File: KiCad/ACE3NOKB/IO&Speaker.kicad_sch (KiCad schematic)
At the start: 22 parts, among them Q3 BC183

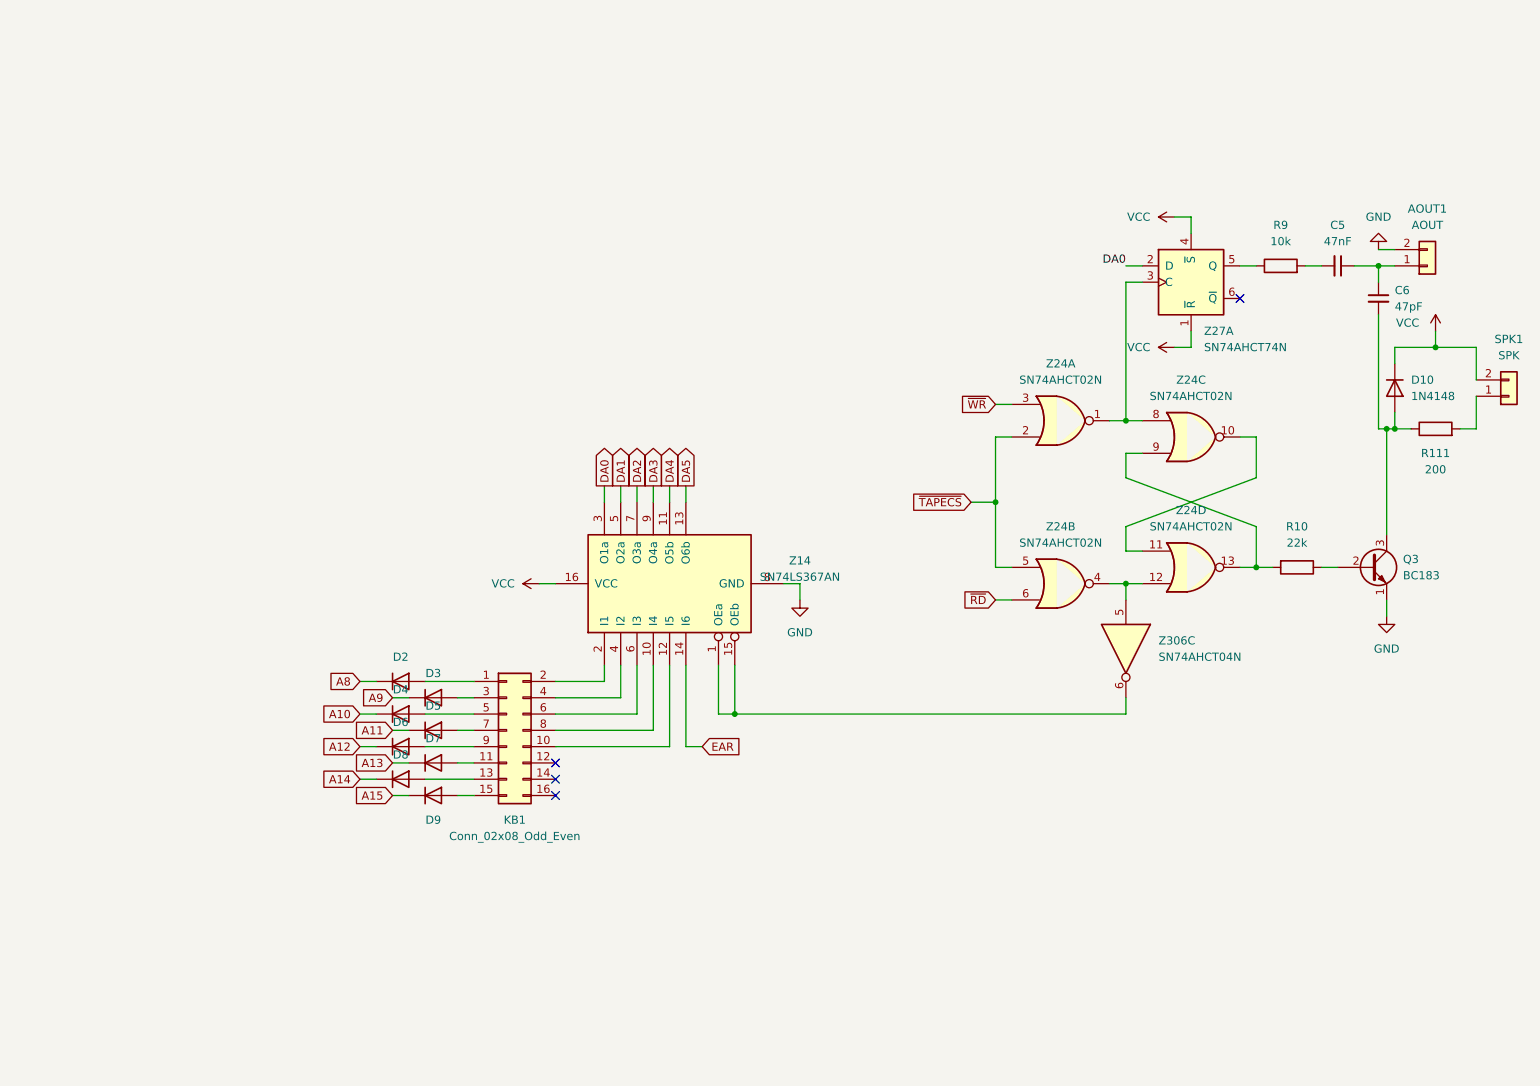
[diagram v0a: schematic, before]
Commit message: Update to latest symbols. Change name of Data Bus from DA to D.
Signed-off-by: John Bradley <flypie@rocketmail.com>
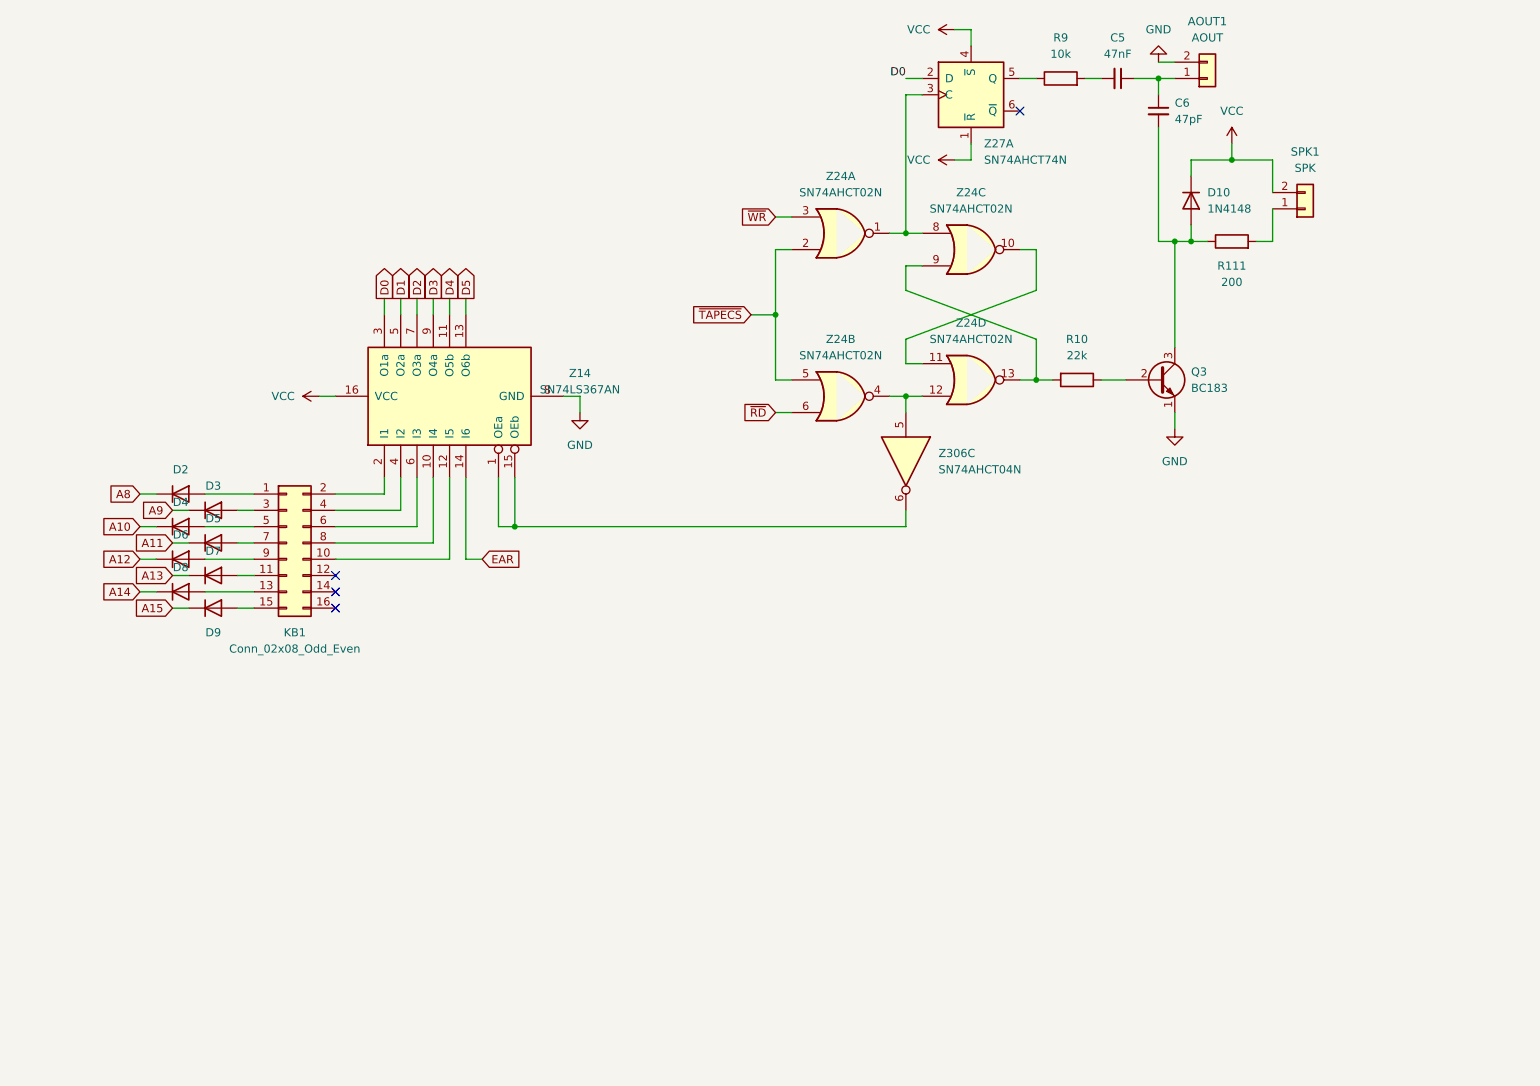
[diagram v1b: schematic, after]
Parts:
- D10: footprint Diode_THT:D_DO-35_SOD27_P2.54mm_Vertical_AnodeUp -> Diode_THT:D_DO-35_SOD27_P7.62mm_Horizontal
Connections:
- net DA0 renamed D0
- net DA1 renamed D1
- net DA2 renamed D2
- net DA3 renamed D3
- net DA4 renamed D4
- net DA5 renamed D5
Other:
- moved on the sheet: AOUT1, C5, C6, D10, D2, D3, D4, D5, D6, D7, D8, D9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

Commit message: Consolidation with increased configuration of speed and Int Routing to allow Orginal ACE ROM.
Signed-off-by: John Bradley <flypie@rocketmail.com>
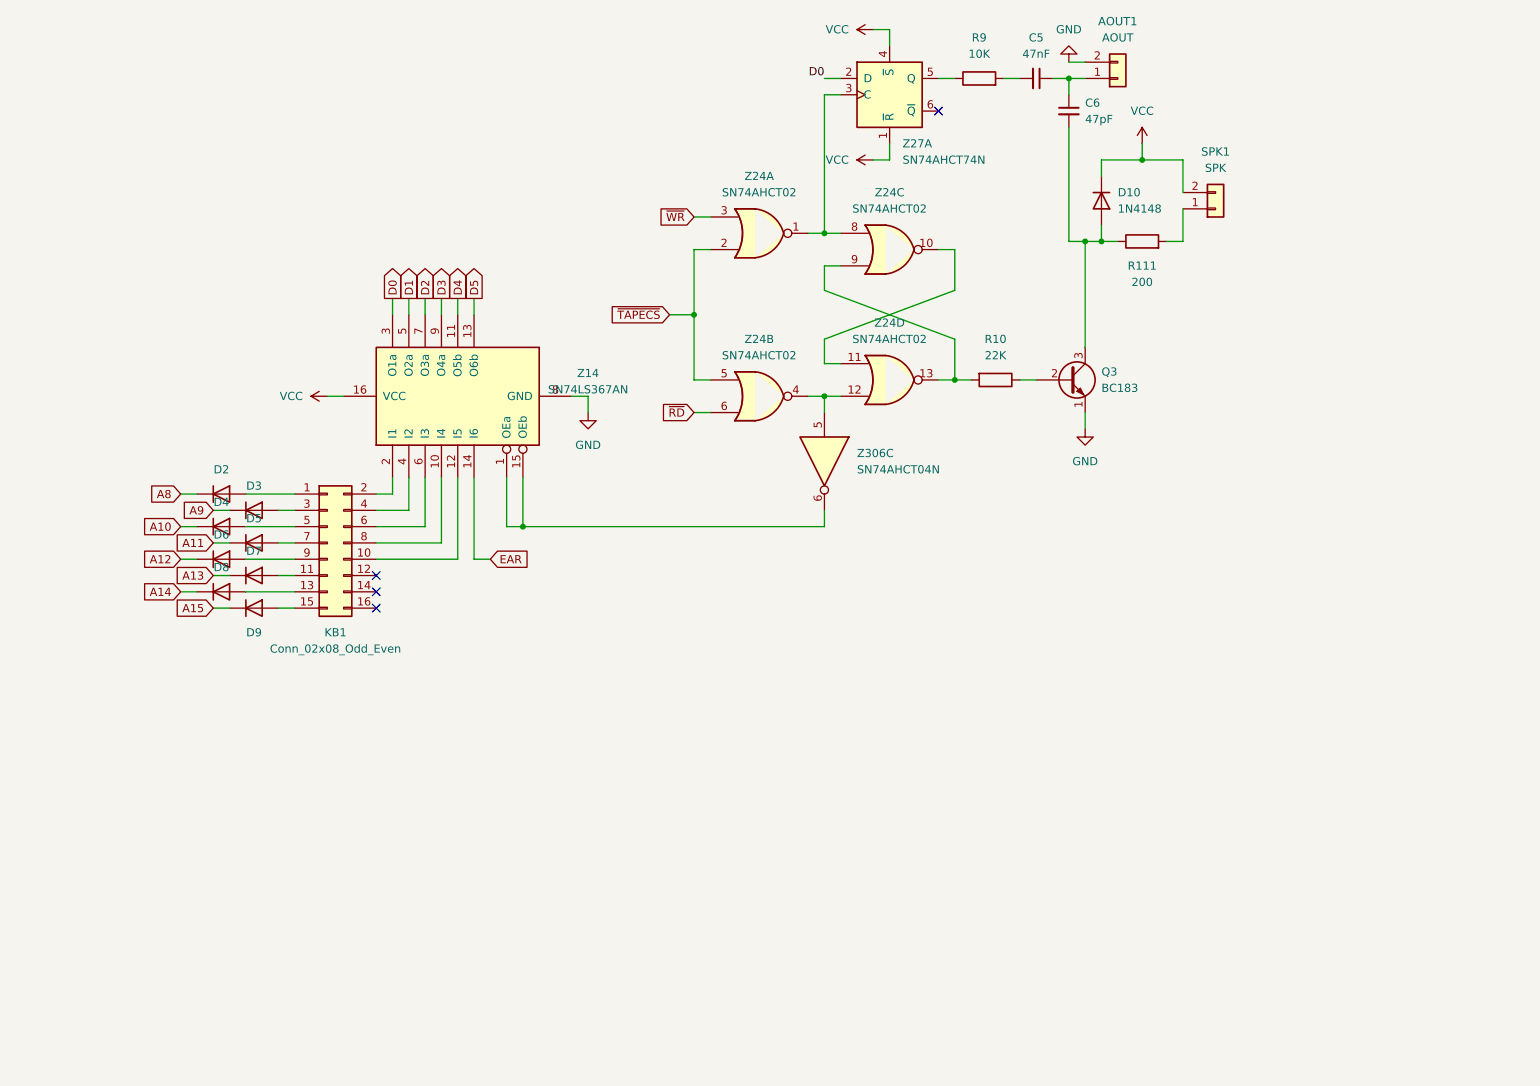
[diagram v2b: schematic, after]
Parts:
- AOUT1, SPK1: Manufacturer_Name TE Connectivity / AMP -> (none); Manufacturer_Part_Number 5-146871-1 -> (none)
- C5: Manufacturer_Name vishay -> (none); Manufacturer_Part_Number K473K15X7RF5TL2 -> (none)
- C6: Manufacturer_Name tdk -> (none); Manufacturer_Part_Number FA18C0G1H470JNU00 -> (none)
- D10: footprint Diode_THT:D_DO-35_SOD27_P7.62mm_Horizontal -> Diode_THT:D_DO-35_SOD27_P2.54mm_Vertical_AnodeUp; Manufacturer_Name ON Semiconductor -> (none); Manufacturer_Part_Number 1N4148 -> (none)
- D2, D3, D4, D5, D6, D7, D8, D9: Manufacturer_Name ON Semiconductor -> (none); Manufacturer_Part_Number 1N4148 -> (none)
- KB1: Manufacturer_Name HARWIN -> (none); Manufacturer_Part_Number M20-9980446 -> (none)
- Q3: Manufacturer_Part_Number BC183 -> (none)
- R10: value 22k -> 22K; Manufacturer_Name Vishay -> (none); Manufacturer_Part_Number MBA02040C2202FRP00 -> (none)
- R111: Manufacturer_Name Vishay -> (none); Manufacturer_Part_Number MBA02040C2000FRP00 -> (none)
- R9: value 10k -> 10K; Manufacturer_Name Vishay -> (none); Manufacturer_Part_Number MBA02040C1002FRP00 -> (none)
- Z14: Manufacturer_Name Texas Instruments -> (none); Manufacturer_Part_Number SN74LS367AN -> (none)
- Z24: value SN74AHCT02N -> SN74AHCT02; Manufacturer_Name Texas Instruments -> (none); Manufacturer_Part_Number SN74AHCT02N -> (none)
- Z27: Manufacturer_Name Texas Instruments -> (none); Manufacturer_Part_Number SN74AHCT74N -> (none)
- Z306: Manufacturer_Name Texas Instruments -> (none); Manufacturer_Part_Number SN74AHCT04N -> (none)
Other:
- moved on the sheet: AOUT1, C5, C6, D10, D2, D3, D4, D5, D6, D7, D8, D9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

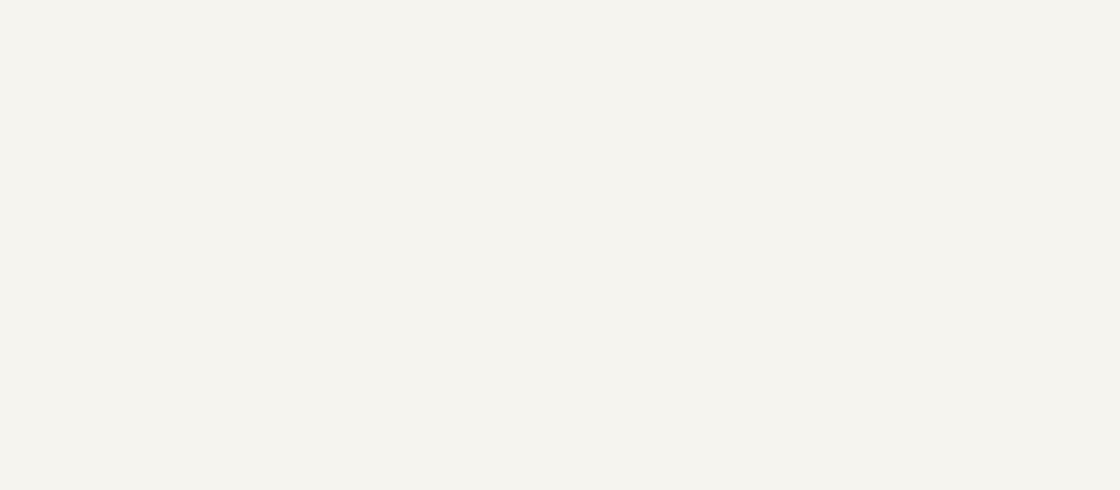
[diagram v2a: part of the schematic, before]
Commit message: Fix mistake with ROM Select.
Signed-off-by: John Bradley <flypie@rocketmail.com>
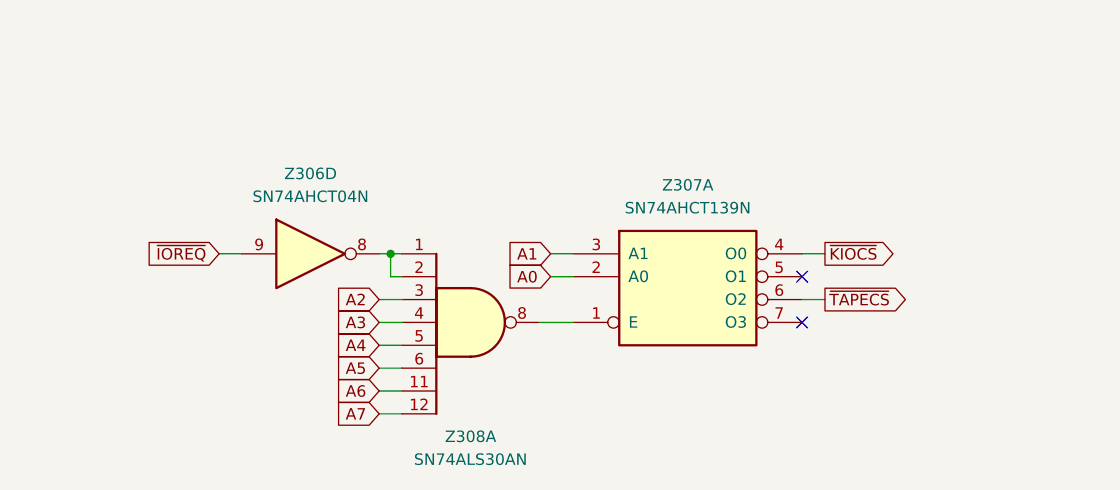
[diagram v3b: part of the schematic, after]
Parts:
- added unit 4 of Z306
- added Z307: SN74AHCT139N, Package_DIP:DIP-16_W7.62mm, symbol 74xx:74LS139
- added Z308: SN74ALS30AN, Package_DIP:DIP-14_W7.62mm, symbol 74xx-FIX:74LS30
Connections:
- net ~{TAPECS}: now also Z307.6 (O2)
- new net: Z306.8, Z308.1, Z308.2
- new net: Z307.1 (E), Z308.8
- new net A0: Z307.2 (A0)
- new net A1: Z307.3 (A1)
- new net A2: Z308.3
- new net A3: Z308.4
- new net A4: Z308.5
- new net A5: Z308.6
- new net A6: Z308.11
- new net A7: Z308.12
- new net ~{IOREQ}: Z306.9
- new net ~{KIOCS}: Z307.4 (O0)
- no-connect marks 4 -> 6

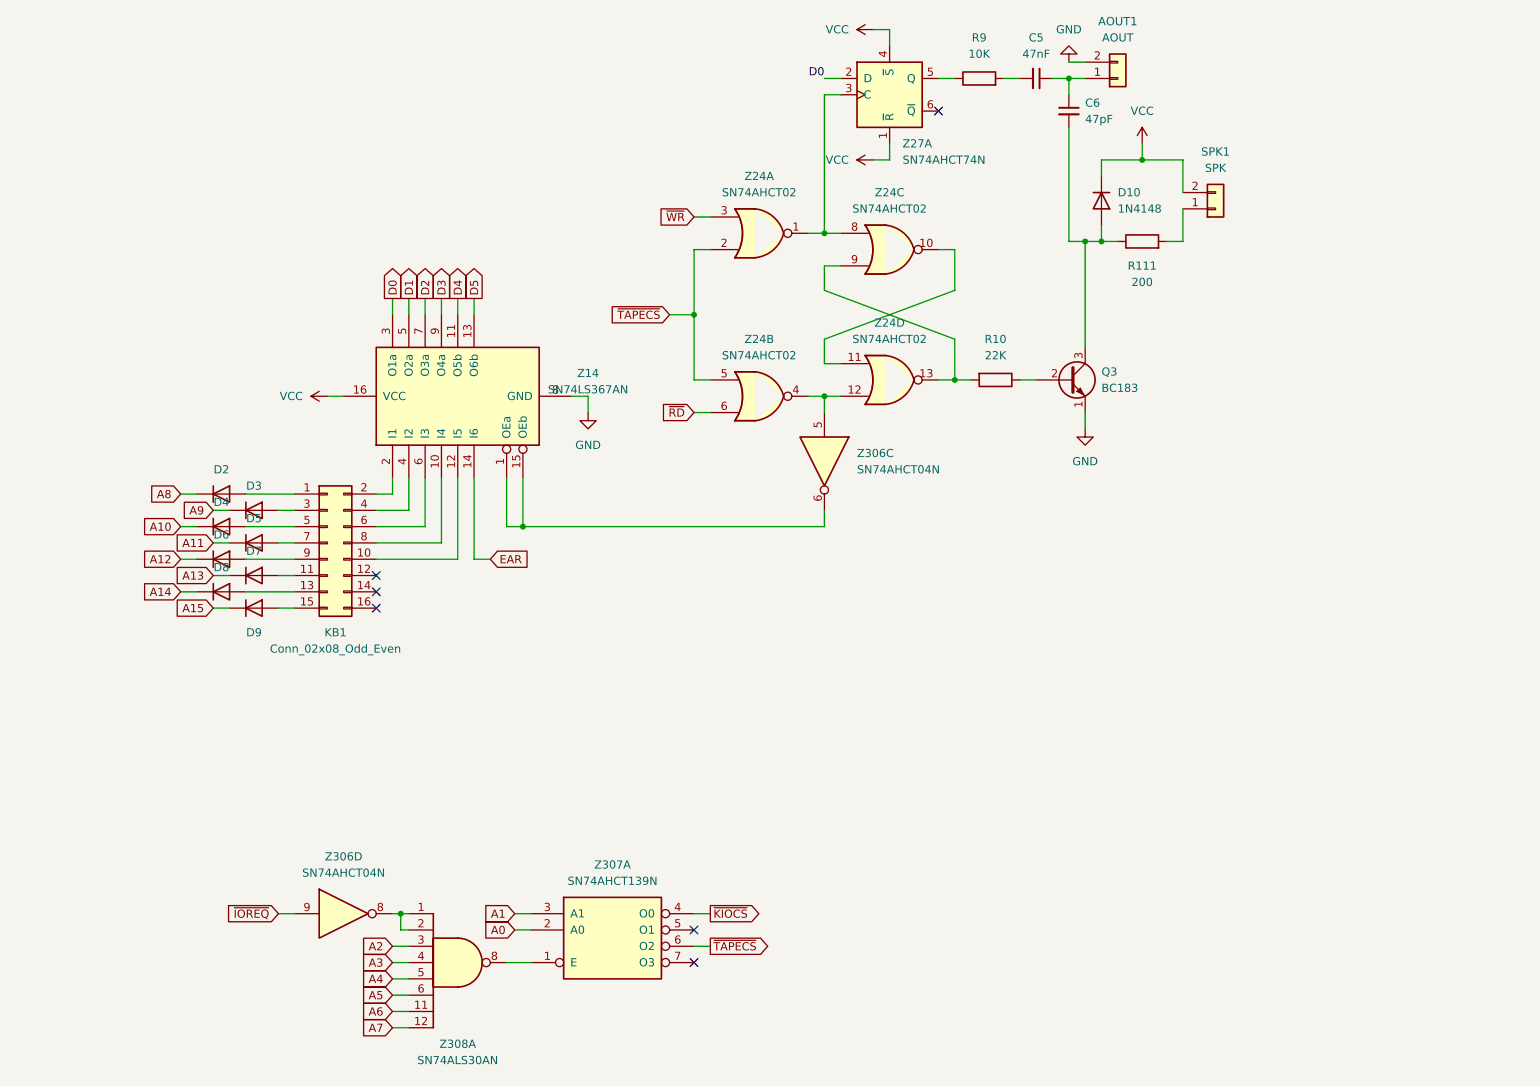
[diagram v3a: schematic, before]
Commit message: Update to last expermintal version. Uses clock sythsiser and can be switched between full ACE compatible and inhanced IO. Should be able to switch between multiple ROM images tosred on the same chip.
Signed-off-by: John Bradley <flypie@rocketmail.com>
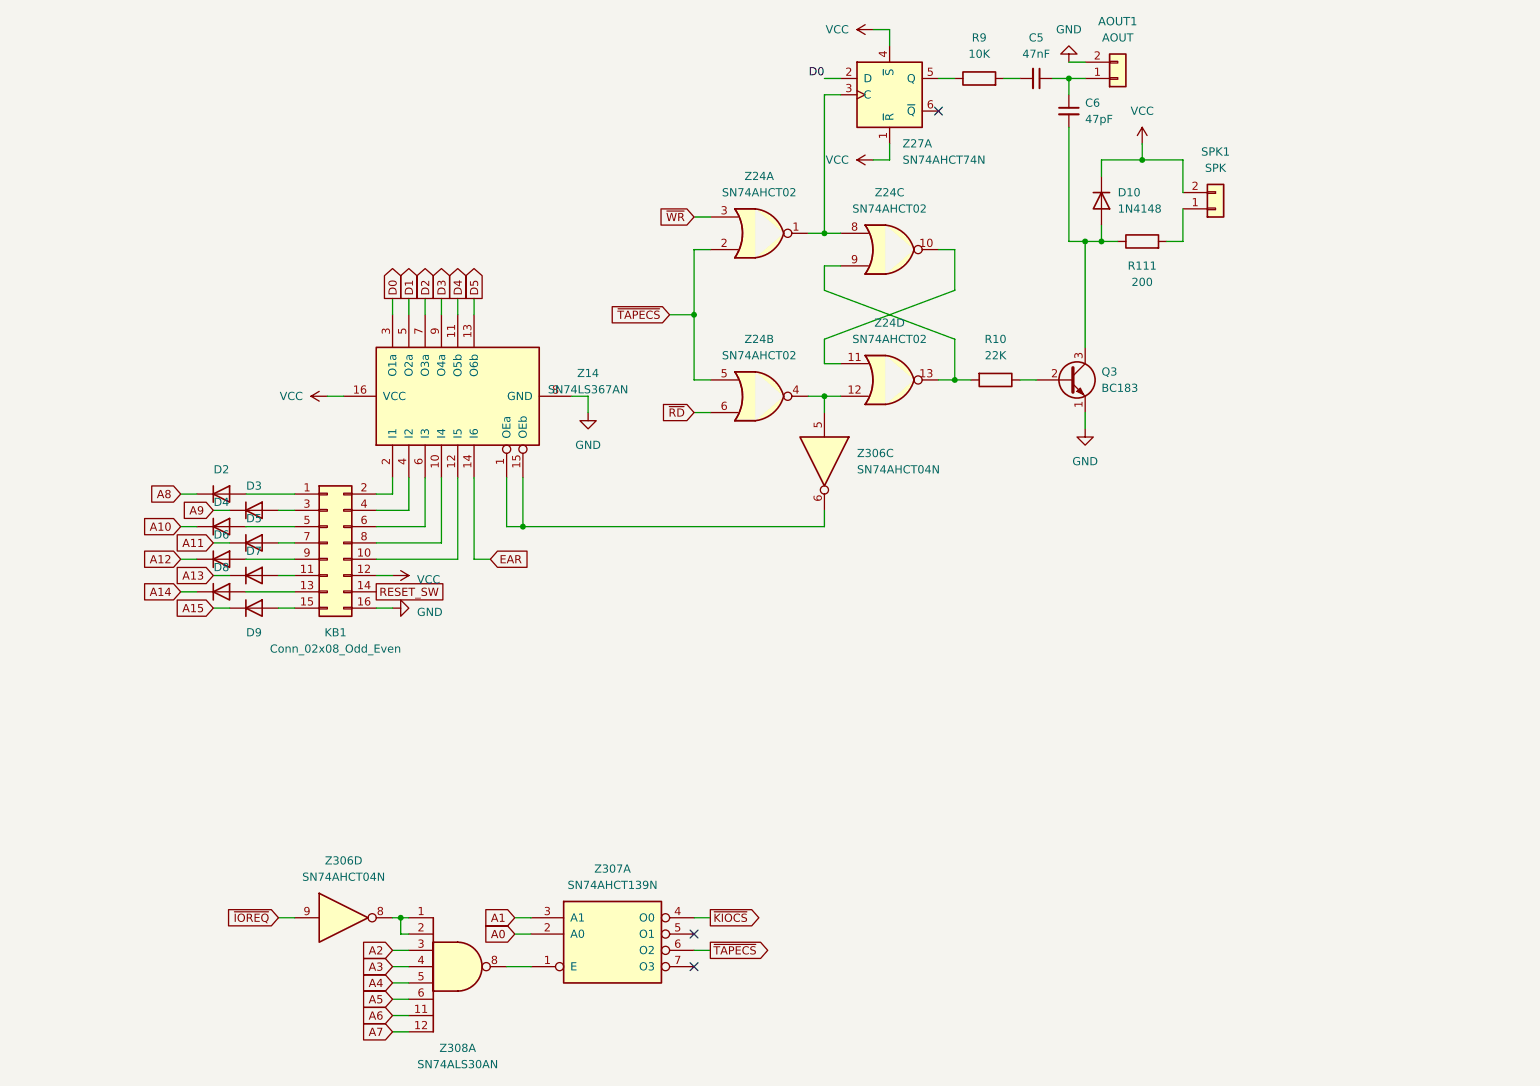
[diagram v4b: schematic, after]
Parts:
- Q3: footprint Package_TO_SOT_THT:TO-92L_Inline_Wide -> Package_TO_SOT_THT:TO-92L_Wide
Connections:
- net GND: now also KB1.16 (Pin_16)
- net VCC: now also KB1.12 (Pin_12)
- net RESET_SW: now reaches KB1.14 (Pin_14)
- no-connect marks 6 -> 3
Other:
- moved on the sheet: Z306D, Z307A, Z308A
